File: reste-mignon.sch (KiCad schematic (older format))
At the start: 0 parts

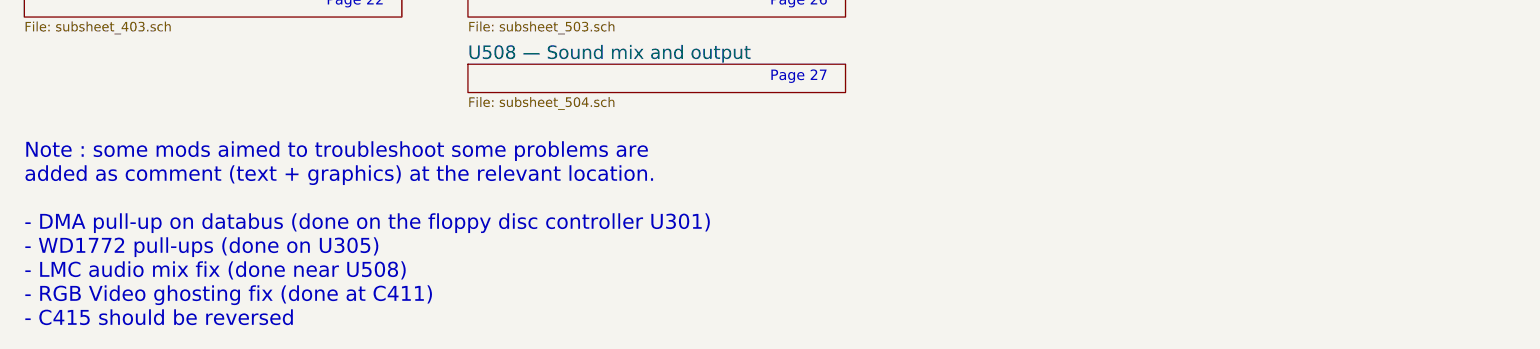
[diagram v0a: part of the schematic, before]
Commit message: rename files as 'reste-mignon'
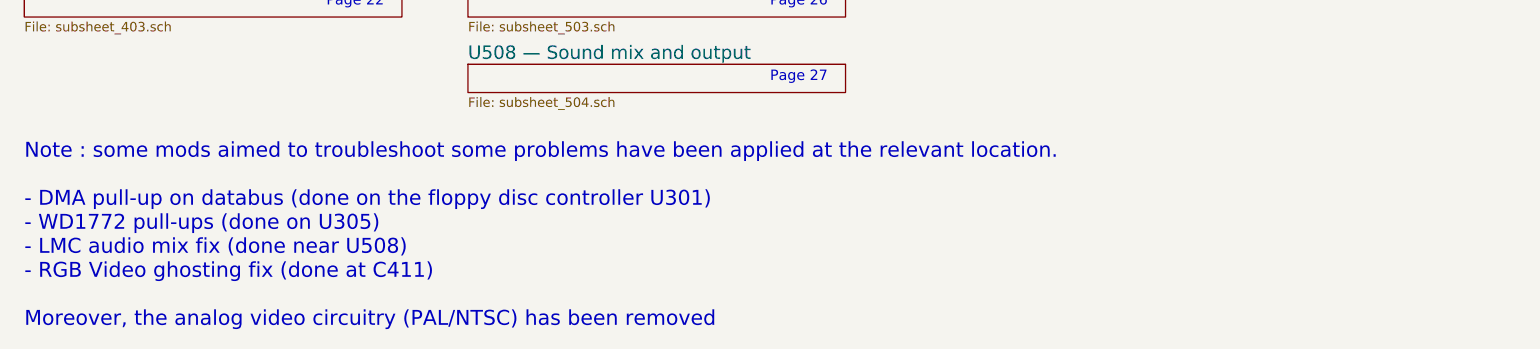
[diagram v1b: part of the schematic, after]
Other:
- note added: "Note : some mods aimed to troubleshoot some problems have been applied at the relevant location.\n\n- DMA pull-up on databus (done on the floppy disc controller U301)\n- WD1772 pull-ups (done on U305)\n- LMC audio mix fix (done near U508)\n- RGB Video ghosting fix (done at C411)\n\nMoreover, the analog video circuitry (PAL/NTSC) has been removed\n"
- note removed: "Note : some mods aimed to troubleshoot some problems are \nadded as comment (text + graphics) at the relevant location.\n\n- DMA pull-up on databus (done on the floppy disc controller U301)\n- WD1772 pull-ups (done on U305)\n- LMC audio mix fix (done near U508)\n- RGB Video ghosting fix (done at C411)\n- C415 should be reversed\n"
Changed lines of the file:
@@
 encoding utf-8
 Sheet 1 29
-Title "Converted schematics of Atari STE"
-Date "2021-08-31"
-Rev "1.0.0"
-Comp ""
-Comment1 "Reference : C300780-001"
-Comment2 ""
-Comment3 ""
-Comment4 ""
+Title "ReSTe mignon"
+Date "2022-02-15"
+Rev "mk0-0"
+Comp "David SPORN"
+Comment1 ""
+Comment2 "a target size of 25×18cm (B5)"
+Comment3 "with some fixes applied and"
+Comment4 "A remake of the Atari STe"
 $EndDescr
 Text Notes 750  2200 0    157  ~ 0
@@
 Table of content
 Text Notes 800  8900 0    79   ~ 0
-Note : some mods aimed to troubleshoot some problems are \nadded as comment (text + graphics) at the relevant location.\n\n- DMA pull-up on databus (done on the floppy disc controller U301)\n- WD1772 pull-ups (done on U305)\n- LMC audio mix fix (done near U508)\n- RGB Video ghosting fix (done at C411)\n- C415 should be reversed\n
+Note : some mods aimed to troubleshoot some problems have been applied at the relevant location.\n\n- DMA pull-up on databus (done on the floppy disc controller U301)\n- WD1772 pull-ups (done on U305)\n- LMC audio mix fix (done near U508)\n- RGB Video ghosting fix (done at C411)\n\nMoreover, the analog video circuitry (PAL/NTSC) has been removed\n
 $EndSCHEMATC
